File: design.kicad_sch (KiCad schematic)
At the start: 159 parts, among them J301 TYPE-C-31-M-12, U1 TTP223, U10 ATtiny1616-M, U2 TTP223, U3 TTP223, U4 TTP223, U5 TTP223, U6 TTP223, U7 TTP223, U8 TTP223

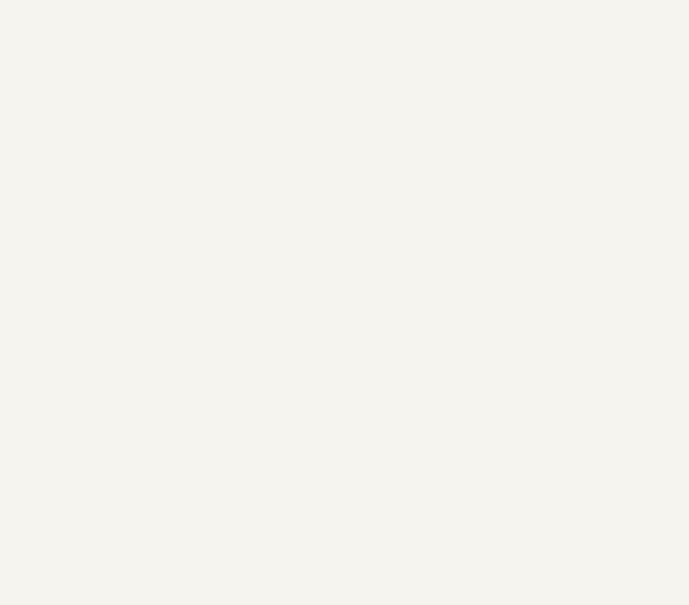
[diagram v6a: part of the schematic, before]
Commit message: mounting holes
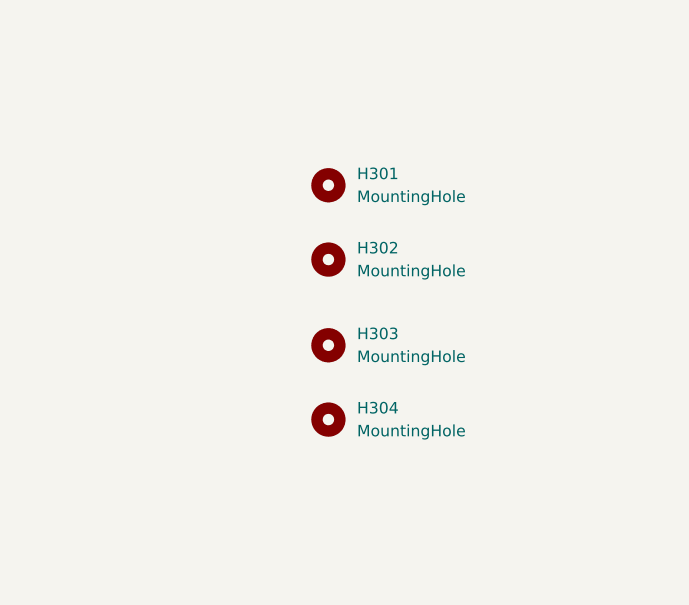
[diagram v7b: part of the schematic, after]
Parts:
- added H301, H302, H303, H304: MountingHole, MountingHole:MountingHole_2.7mm_M2.5, symbol Mechanical:MountingHole
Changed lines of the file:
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@@
     (pin "1")
   )
+  (symbol (lib_id "Mechanical:MountingHole") (at 528.955 364.49 0) (unit 1)
+    (in_bom yes) (on_board yes) (fields_autoplaced)
+    (property "Reference" "H304" (id 0) (at 532.13 363.2199 0)
+      (effects (font (size 1.27 1.27)) (justify left))
+    )
+    (property "Value" "MountingHole" (id 1) (at 532.13 365.7599 0)
+      (effects (font (size 1.27 1.27)) (justify left))
+    )
+    (property "Footprint" "MountingHole:MountingHole_2.7mm_M2.5" (id 2) (at 528.955 364.49 0)
+      (effects (font (size 1.27 1.27)) hide)
+    )
+    (property "Datasheet" "~" (id 3) (at 528.955 364.49 0)
+      (effects (font (size 1.27 1.27)) hide)
+    )
+  )
   (symbol (lib_id "power:GND") (at 369.57 153.67 0) (unit 1)
     (in_bom yes) (on_board yes)
@@
     (pin "1")
   )
+  (symbol (lib_id "Mechanical:MountingHole") (at 528.955 356.235 0) (unit 1)
+    (in_bom yes) (on_board yes) (fields_autoplaced)
+    (property "Reference" "H303" (id 0) (at 532.13 354.9649 0)
+      (effects (font (size 1.27 1.27)) (justify left))
+    )
+    (property "Value" "MountingHole" (id 1) (at 532.13 357.5049 0)
+      (effects (font (size 1.27 1.27)) (justify left))
+    )
+    (property "Footprint" "MountingHole:MountingHole_2.7mm_M2.5" (id 2) (at 528.955 356.235 0)
+      (effects (font (size 1.27 1.27)) hide)
+    )
+    (property "Datasheet" "~" (id 3) (at 528.955 356.235 0)
+      (effects (font (size 1.27 1.27)) hide)
+    )
+  )
   (symbol (lib_id "Device:C_Small") (at 196.215 275.59 0) (unit 1)
     (in_bom yes) (on_board yes)
@@
     (pin "1")
   )
+  (symbol (lib_id "Mechanical:MountingHole") (at 528.955 338.455 0) (unit 1)
+    (in_bom yes) (on_board yes) (fields_autoplaced)
+    (property "Reference" "H301" (id 0) (at 532.13 337.1849 0)
+      (effects (font (size 1.27 1.27)) (justify left))
+    )
+    (property "Value" "MountingHole" (id 1) (at 532.13 339.7249 0)
+      (effects (font (size 1.27 1.27)) (justify left))
+    )
+    (property "Footprint" "MountingHole:MountingHole_2.7mm_M2.5" (id 2) (at 528.955 338.455 0)
+      (effects (font (size 1.27 1.27)) hide)
+    )
+    (property "Datasheet" "~" (id 3) (at 528.955 338.455 0)
+      (effects (font (size 1.27 1.27)) hide)
+    )
+  )
   (symbol (lib_id "power:GND") (at 64.135 342.265 0) (unit 1)
     (in_bom yes) (on_board yes)
@@
     (pin "1")
   )
+  (symbol (lib_id "Mechanical:MountingHole") (at 528.955 346.71 0) (unit 1)
+    (in_bom yes) (on_board yes) (fields_autoplaced)
+    (property "Reference" "H302" (id 0) (at 532.13 345.4399 0)
+      (effects (font (size 1.27 1.27)) (justify left))
+    )
+    (property "Value" "MountingHole" (id 1) (at 532.13 347.9799 0)
+      (effects (font (size 1.27 1.27)) (justify left))
+    )
+    (property "Footprint" "MountingHole:MountingHole_2.7mm_M2.5" (id 2) (at 528.955 346.71 0)
+      (effects (font (size 1.27 1.27)) hide)
+    )
+    (property "Datasheet" "~" (id 3) (at 528.955 346.71 0)
+      (effects (font (size 1.27 1.27)) hide)
+    )
+  )
   (symbol (lib_name "WS2812B_28") (lib_id "LED:WS2812B") (at 435.61 199.39 0) (unit 1)
     (in_bom yes) (on_board yes)
@@
       (reference "D102") (unit 1) (value "Green") (footprint "LED_SMD:LED_0603_1608Metric")
     )
+    (path "/b8463139-d8e2-4e6f-862e-d915ef289892"
+      (reference "H301") (unit 1) (value "MountingHole") (footprint "MountingHole:MountingHole_2.7mm_M2.5")
+    )
+    (path "/f507f108-ae1c-4cd2-aa19-789f2a6d5724"
+      (reference "H302") (unit 1) (value "MountingHole") (footprint "MountingHole:MountingHole_2.7mm_M2.5")
+    )
+    (path "/9e682446-ace6-4349-9567-b0ebd0dd40b9"
+      (reference "H303") (unit 1) (value "MountingHole") (footprint "MountingHole:MountingHole_2.7mm_M2.5")
+    )
+    (path "/0c00fd02-a304-4575-bcf1-b01798687af8"
+      (reference "H304") (unit 1) (value "MountingHole") (footprint "MountingHole:MountingHole_2.7mm_M2.5")
+    )
     (path "/49f496c5-52ef-4d33-b13c-79b5ef9a1e3c"
